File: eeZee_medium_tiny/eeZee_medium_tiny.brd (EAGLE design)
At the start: 30 x 17.8 mm, 11 parts, among them IC1 TINY24/44/84, J2 avrisp, Q1 16MHz

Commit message: Minor board tweaks
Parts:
- flipped JP4 to the bottom, turned to 180 degrees
- flipped JP5 to the bottom, turned to 0 degrees
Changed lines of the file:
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@@
 <setting verticaltext="up"/>
 </settings>
-<grid distance="10" unitdist="mil" unit="inch" style="lines" multiple="1" display="no" altdistance="0.005" altunitdist="inch" altunit="inch"/>
+<grid distance="10" unitdist="mil" unit="mm" style="lines" multiple="1" display="no" altdistance="0.005" altunitdist="inch" altunit="inch"/>
 <layers>
 <layer number="1" name="Top" color="4" fill="1" visible="yes" active="yes"/>
@@
 <attribute name="VALUE" x="4.699" y="6.985" size="1.27" layer="27" ratio="10"/>
 </element>
-<element name="JP4" library="pinhead-2" package="1X07-S" value="" x="11.43" y="2.54" smashed="yes">
-<attribute name="VALUE" x="2.54" y="-0.635" size="1.27" layer="27"/>
-</element>
-<element name="JP5" library="pinhead-2" package="1X07-S" value="" x="11.43" y="15.24" smashed="yes" rot="R180">
-<attribute name="VALUE" x="20.32" y="18.415" size="1.27" layer="27" rot="R180"/>
+<element name="JP4" library="pinhead-2" package="1X07-S" value="" x="11.43" y="2.54" smashed="yes" rot="MR180">
+<attribute name="VALUE" x="2.54" y="5.715" size="1.27" layer="28" rot="MR180"/>
+</element>
+<element name="JP5" library="pinhead-2" package="1X07-S" value="" x="11.43" y="15.24" smashed="yes" rot="MR0">
+<attribute name="VALUE" x="20.32" y="12.065" size="1.27" layer="28" rot="MR0"/>
 </element>
 </elements>
@@
 <contactref element="IC1" pad="1"/>
 <contactref element="IC1" pad="1"/>
-<wire x1="3.81" y1="2.54" x2="3.81" y2="5.08" width="0.254" layer="1"/>
 <wire x1="3.81" y1="5.08" x2="3.556" y2="5.08" width="0.254" layer="16"/>
 <wire x1="3.556" y1="5.08" x2="2.286" y2="6.35" width="0.254" layer="16"/>
@@
 <wire x1="16.344" y1="8.89" x2="16.51" y2="8.724" width="0.254" layer="16"/>
 <wire x1="16.51" y1="8.724" x2="17.106" y2="8.724" width="0.254" layer="16"/>
+<wire x1="3.81" y1="2.54" x2="3.81" y2="5.08" width="0.254" layer="1"/>
 </signal>
 <signal name="!RESET">
@@
 <contactref element="IC1" pad="4"/>
 <contactref element="JP4" pad="4"/>
-<wire x1="11.43" y1="2.54" x2="11.43" y2="5.08" width="0.254" layer="1"/>
 <wire x1="21.896" y1="5.806" x2="28.396" y2="5.806" width="0.254" layer="1"/>
 <wire x1="24.384" y1="10.922" x2="21.896" y2="8.434" width="0.254" layer="1"/>
 <wire x1="21.896" y1="5.806" x2="21.896" y2="8.434" width="0.254" layer="1"/>
-<wire x1="21.186" y1="6.516" x2="21.471" y2="6.231" width="0.254" layer="16"/>
-<wire x1="21.471" y1="6.231" x2="21.896" y2="5.806" width="0.254" layer="16"/>
 <wire x1="16.51" y1="7.024" x2="14.136" y2="7.024" width="0.254" layer="16"/>
 <wire x1="14.136" y1="7.024" x2="12.192" y2="5.08" width="0.254" layer="16"/>
 <wire x1="12.192" y1="5.08" x2="11.43" y2="5.08" width="0.254" layer="16"/>
 <wire x1="16.51" y1="7.024" x2="20.678" y2="7.024" width="0.254" layer="16"/>
-<wire x1="20.678" y1="7.024" x2="21.186" y2="6.516" width="0.254" layer="16"/>
+<wire x1="20.678" y1="7.024" x2="21.896" y2="5.806" width="0.254" layer="16"/>
+<wire x1="11.43" y1="2.54" x2="11.43" y2="5.08" width="0.254" layer="1"/>
 </signal>
 <signal name="XTAL2">
@@
 <contactref element="IC1" pad="3"/>
 <contactref element="JP4" pad="3"/>
-<wire x1="8.89" y1="2.54" x2="8.89" y2="5.08" width="0.254" layer="1"/>
 <wire x1="10.58" y1="7.112" x2="10.58" y2="6.77" width="0.254" layer="16"/>
 <wire x1="10.58" y1="6.77" x2="8.89" y2="5.08" width="0.254" layer="16"/>
 <wire x1="10.58" y1="7.112" x2="10.58" y2="7.564" width="0.254" layer="16"/>
 <wire x1="10.58" y1="7.564" x2="12.668" y2="9.652" width="0.254" layer="16"/>
+<wire x1="8.89" y1="2.54" x2="8.89" y2="5.08" width="0.254" layer="1"/>
 </signal>
 <signal name="XTAL1">
@@
 <contactref element="IC1" pad="2"/>
 <contactref element="JP4" pad="2"/>
-<wire x1="6.35" y1="2.54" x2="6.35" y2="5.08" width="0.254" layer="1"/>
 <wire x1="7.024" y1="7.112" x2="7.024" y2="8.008" width="0.254" layer="16"/>
 <wire x1="7.024" y1="8.008" x2="8.668" y2="9.652" width="0.254" layer="16"/>
 <wire x1="7.024" y1="7.112" x2="7.024" y2="5.754" width="0.254" layer="16"/>
 <wire x1="7.024" y1="5.754" x2="6.35" y2="5.08" width="0.254" layer="16"/>
+<wire x1="6.35" y1="2.54" x2="6.35" y2="5.08" width="0.254" layer="1"/>
 </signal>
 <signal name="N$1">
@@
 <contactref element="JP4" pad="7"/>
 <contactref element="J2" pad="4"/>
-<wire x1="19.05" y1="2.54" x2="19.05" y2="5.08" width="0.254" layer="1"/>
 <wire x1="19.05" y1="5.08" x2="19.05" y2="8.128" width="0.254" layer="1"/>
 <wire x1="19.05" y1="8.128" x2="23.114" y2="12.192" width="0.254" layer="1"/>
 <wire x1="23.114" y1="12.192" x2="25.654" y2="12.192" width="0.254" layer="1"/>
 <wire x1="25.654" y1="12.192" x2="26.924" y2="13.462" width="0.254" layer="1"/>
+<wire x1="19.05" y1="2.54" x2="19.05" y2="5.08" width="0.254" layer="1"/>
 </signal>
 <signal name="MISO">
@@
 <contactref element="JP5" pad="1"/>
 <contactref element="J2" pad="1"/>
-<wire x1="19.05" y1="12.7" x2="19.05" y2="15.24" width="0.254" layer="1"/>
 <wire x1="24.384" y1="16.002" x2="19.812" y2="16.002" width="0.254" layer="1"/>
 <wire x1="19.812" y1="16.002" x2="19.05" y2="15.24" width="0.254" layer="1"/>
+<wire x1="19.05" y1="15.24" x2="19.05" y2="12.7" width="0.254" layer="1"/>
 </signal>
 <signal name="SCK">
@@
 <contactref element="JP5" pad="2"/>
 <contactref element="J2" pad="3"/>
-<wire x1="16.51" y1="12.7" x2="16.51" y2="15.24" width="0.254" layer="1"/>
 <wire x1="16.51" y1="12.7" x2="18.034" y2="11.176" width="0.254" layer="1"/>
 <wire x1="18.034" y1="11.176" x2="20.828" y2="11.176" width="0.254" layer="1"/>
 <wire x1="20.828" y1="11.176" x2="23.114" y2="13.462" width="0.254" layer="1"/>
 <wire x1="23.114" y1="13.462" x2="24.384" y2="13.462" width="0.254" layer="1"/>
+<wire x1="16.51" y1="15.24" x2="16.51" y2="12.7" width="0.254" layer="1"/>
 </signal>
 <signal name="N$8">
 <contactref element="IC1" pad="10"/>
 <contactref element="JP5" pad="3"/>
-<wire x1="13.97" y1="12.7" x2="13.97" y2="15.24" width="0.254" layer="1"/>
+<wire x1="13.97" y1="15.24" x2="13.97" y2="12.7" width="0.254" layer="1"/>
 </signal>
 <signal name="N$9">

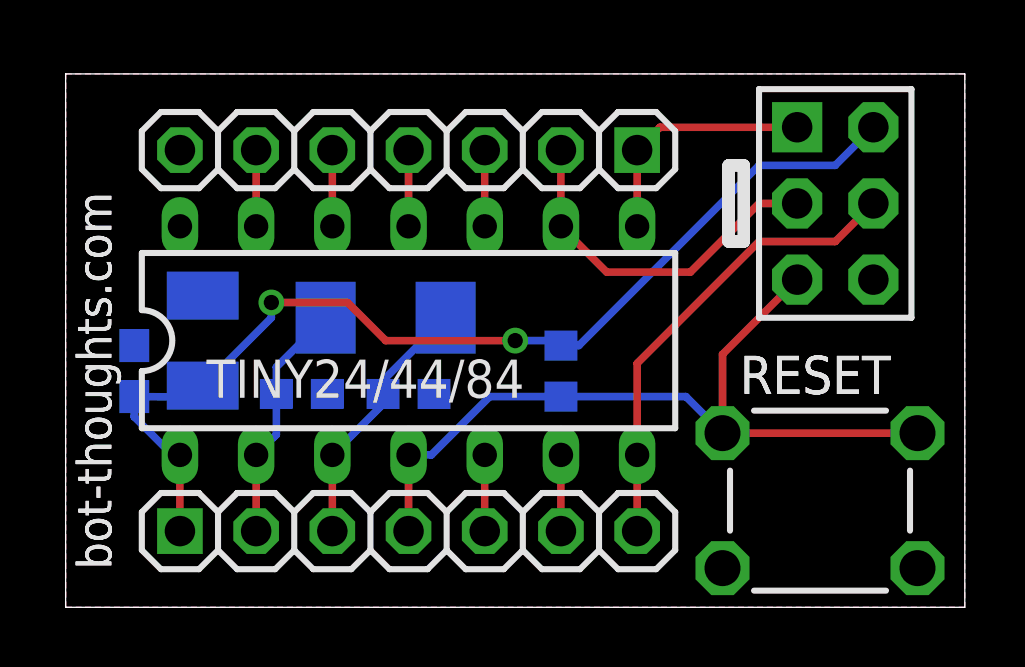
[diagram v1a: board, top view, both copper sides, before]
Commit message: Rev 0.2 as ordered, mitered corners, flipped tantalum and added polarity silk screen, changed location of caps/crystals for easier assembly, shrunk board size.
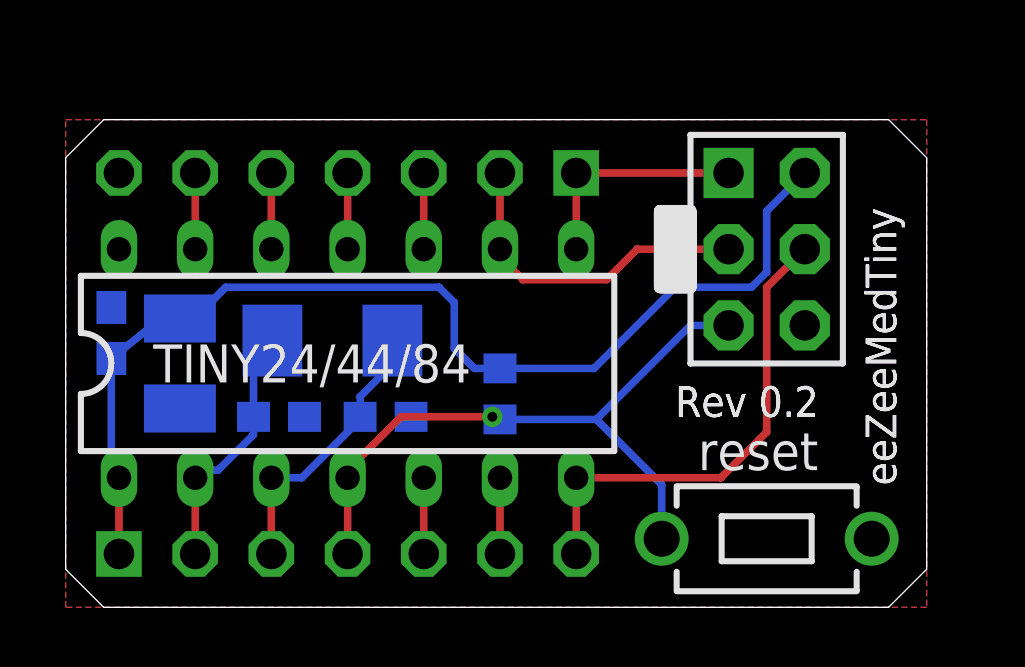
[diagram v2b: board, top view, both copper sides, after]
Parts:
- removed S2: RESET, mes_electromech:6MMTACTILE_4PIN
- added S1: reset, mes_electromech:6MMTACTILE_RECT
- C2: device rcl:SMC_B -> mes_rcl:SMC_B
- moved J2 2.75 mm to (23.4, 11.9)
- moved R1 2.17 mm to (14.5, 7.11)
- moved IC1 2.17 mm to (9.40, 8.13)
- moved JP5 2.17 mm to (9.40, 14.5)
- moved JP4 2.17 mm to (9.40, 1.78)
- moved Q1 1.93 mm to (8.89, 8.89)
- moved C1 1.48 mm to (1.52, 9.14)
- moved C4 1.08 mm to (10.7, 6.35)
- moved C2 1.08 mm to (3.81, 8.13), turned to 270 degrees
- moved C5 1.08 mm to (7.11, 6.35)
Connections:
- net !RESET: now also S1.P$2; no longer S2.B1, S2.B2
- net GND: now also S1.P$1; no longer S2.A1, S2.A2
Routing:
- net !RESET: track 27.0 -> 22.4 mm, vias 0 -> 1
- net VCC: track 35.1 -> 36.5 mm, vias 2 -> 0
- net SCK: track 12.0 -> 11.2 mm
- net XTAL2: track 8.68 -> 9.38 mm
- net MISO: track 8.19 -> 7.62 mm
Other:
- board size 30 x 17.8 mm -> 28.7 x 16.3 mm
- board text added: "Rev 0.2"
- board text added: "eeZeeMedTiny"
- board text added: "reset"
- board text removed: "C1"
- board text removed: "C2"
- board text removed: "C4"
- board text removed: "C5"
- board text removed: "Q1"
- board text removed: "R1"
- board text removed: "RESET"
- board text removed: "Rev 0.1"
